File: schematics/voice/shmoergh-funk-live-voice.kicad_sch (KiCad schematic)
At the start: 26 parts, among them Q1 2N3904, U2 TL074, U4 TL074

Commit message: Minor updates
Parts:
- C2: value 270p -> 470p
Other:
- note added: "Discharge RC = 10k * 470pF = 4.7us Could go with 560p too"
- note removed: "Discharge RC = 10k * 270pF = 2.7us"
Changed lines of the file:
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@@
     (effects (font (size 1.27 1.27)) (justify left bottom))
   )
-  (text "Discharge RC = 10k * 270pF = 2.7us" (at 99.06 22.86 0)
+  (text "Discharge RC = 10k * 470pF = 4.7us\nCould go with 560p too"
+    (at 99.06 22.86 0)
     (effects (font (size 1.27 1.27)) (justify left bottom))
   )
@@
       (effects (font (size 1.27 1.27)))
     )
-    (property "Value" "270p" (at 119.38 28.9306 90)
+    (property "Value" "470p" (at 119.38 28.9306 90)
       (effects (font (size 1.27 1.27)))
     )

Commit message: Updated DCO
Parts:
- C2: value 470p -> 560
- R15: value 5.6k -> 20k
- R16: value 20k -> 10k
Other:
- note added: "Integrator's RC constant for max frequency of 5kHz RC = 1 / 5kHz = 0.2ms If any of these components are changed then the code should also be updated (the PWM's output is calculated with a max frequency that's set by these components)."
- note added: "Integrator's discharge constant RCdis = 2.2k * 1nF = 2.2us"
- note added: "Output = 6Vpp"
- note added: "Output aplification A = 1+1 = 2 to have 6.6Vpp"
- note removed: "Integrator's RC constant for max frequency of 5kHz RC = 1 / 5kHz = 0.2ms Integrator's discharge constant RCdis = 2.2k * 1nF = 2.2us"
- note removed: "Output aplification A = 10/3.3 = 3.03 to have 10Vpp"
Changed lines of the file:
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@@
   (junction (at 158.75 77.47) (diameter 0) (color 0 0 0 0)
   )
+  (junction (at 190.5 91.44) (diameter 0) (color 0 0 0 0)
+  )
+  (junction (at 35.56 176.53) (diameter 0) (color 0 0 0 0)
+  )
+  (junction (at 128.27 33.02) (diameter 0) (color 0 0 0 0)
+  )
+  (junction (at 149.86 135.89) (diameter 0) (color 0 0 0 0)
+  )
   (junction (at 158.75 88.9) (diameter 0) (color 0 0 0 0)
-  )
-  (junction (at 190.5 91.44) (diameter 0) (color 0 0 0 0)
-  )
-  (junction (at 35.56 176.53) (diameter 0) (color 0 0 0 0)
-  )
-  (junction (at 128.27 33.02) (diameter 0) (color 0 0 0 0)
-  )
-  (junction (at 149.86 135.89) (diameter 0) (color 0 0 0 0)
   )
   (junction (at 196.85 133.35) (diameter 0) (color 0 0 0 0)
@@
     (stroke (width 0) (type default))
   )
+  (polyline (pts (xy 149.86 66.04) (xy 149.86 67.31))
+    (stroke (width 0) (type dash))
+  )
   (wire (pts (xy 127 124.46) (xy 133.35 124.46))
     (stroke (width 0) (type default))
@@
     (stroke (width 0) (type default))
   )
+  (wire (pts (xy 158.75 88.9) (xy 175.26 88.9))
+    (stroke (width 0) (type default))
+  )
   (wire (pts (xy 224.79 29.21) (xy 251.46 29.21))
     (stroke (width 0) (type default))
@@
     (stroke (width 0) (type default))
   )
+  (polyline (pts (xy 130.81 77.47) (xy 130.81 99.06))
+    (stroke (width 0) (type dash))
+  )
   (wire (pts (xy 175.26 100.33) (xy 175.26 104.14))
     (stroke (width 0) (type default))
@@
     (stroke (width 0) (type default))
   )
+  (wire (pts (xy 128.27 43.18) (xy 128.27 45.72))
+    (stroke (width 0) (type default))
+  )
+  (wire (pts (xy 246.38 41.91) (xy 251.46 41.91))
+    (stroke (width 0) (type default))
+  )
+  (wire (pts (xy 158.75 130.81) (xy 158.75 105.41))
+    (stroke (width 0) (type default))
+  )
+  (wire (pts (xy 158.75 77.47) (xy 158.75 62.23))
+    (stroke (width 0) (type default))
+  )
+  (wire (pts (xy 86.36 83.82) (xy 86.36 86.36))
+    (stroke (width 0) (type default))
+  )
+  (wire (pts (xy 229.87 33.02) (xy 229.87 31.75))
+    (stroke (width 0) (type default))
+  )
+  (wire (pts (xy 194.31 133.35) (xy 196.85 133.35))
+    (stroke (width 0) (type default))
+  )
+  (wire (pts (xy 107.95 33.02) (xy 115.57 33.02))
+    (stroke (width 0) (type default))
+  )
+  (wire (pts (xy 224.79 33.02) (xy 224.79 29.21))
+    (stroke (width 0) (type default))
+  )
+  (wire (pts (xy 144.78 44.45) (xy 140.97 44.45))
+    (stroke (width 0) (type default))
+  )
+  (wire (pts (xy 110.49 66.04) (xy 106.68 66.04))
+    (stroke (width 0) (type default))
+  )
+  (wire (pts (xy 154.94 44.45) (xy 158.75 44.45))
+    (stroke (width 0) (type default))
+  )
+  (wire (pts (xy 106.68 66.04) (xy 106.68 72.39))
+    (stroke (width 0) (type default))
+  )
+  (polyline (pts (xy 124.46 67.31) (xy 149.86 67.31))
+    (stroke (width 0) (type dash))
+  )
+  (wire (pts (xy 134.62 74.93) (xy 140.97 74.93))
+    (stroke (width 0) (type default))
+  )
+  (wire (pts (xy 97.79 72.39) (xy 106.68 72.39))
+    (stroke (width 0) (type default))
+  )
+  (wire (pts (xy 196.85 133.35) (xy 196.85 135.89))
+    (stroke (width 0) (type default))
+  )
+  (wire (pts (xy 246.38 49.53) (xy 251.46 49.53))
+    (stroke (width 0) (type default))
+  )
+  (wire (pts (xy 196.85 133.35) (xy 207.01 133.35))
+    (stroke (width 0) (type default))
+  )
+  (wire (pts (xy 246.38 44.45) (xy 251.46 44.45))
+    (stroke (width 0) (type default))
+  )
+  (wire (pts (xy 140.97 74.93) (xy 142.24 74.93))
+    (stroke (width 0) (type default))
+  )
+  (wire (pts (xy 140.97 44.45) (xy 140.97 62.23))
+    (stroke (width 0) (type default))
+  )
+  (wire (pts (xy 123.19 33.02) (xy 128.27 33.02))
+    (stroke (width 0) (type default))
+  )
   (wire (pts (xy 158.75 88.9) (xy 158.75 97.79))
     (stroke (width 0) (type default))
   )
-  (wire (pts (xy 128.27 43.18) (xy 128.27 45.72))
-    (stroke (width 0) (type default))
-  )
-  (wire (pts (xy 246.38 41.91) (xy 251.46 41.91))
-    (stroke (width 0) (type default))
-  )
-  (wire (pts (xy 158.75 130.81) (xy 158.75 105.41))
-    (stroke (width 0) (type default))
-  )
-  (wire (pts (xy 158.75 77.47) (xy 158.75 62.23))
-    (stroke (width 0) (type default))
-  )
-  (wire (pts (xy 86.36 83.82) (xy 86.36 86.36))
-    (stroke (width 0) (type default))
-  )
-  (wire (pts (xy 229.87 33.02) (xy 229.87 31.75))
-    (stroke (width 0) (type default))
-  )
-  (wire (pts (xy 158.75 88.9) (xy 175.26 88.9))
-    (stroke (width 0) (type default))
-  )
-  (wire (pts (xy 194.31 133.35) (xy 196.85 133.35))
-    (stroke (width 0) (type default))
-  )
-  (wire (pts (xy 107.95 33.02) (xy 115.57 33.02))
-    (stroke (width 0) (type default))
-  )
-  (wire (pts (xy 224.79 33.02) (xy 224.79 29.21))
-    (stroke (width 0) (type default))
-  )
-  (wire (pts (xy 144.78 44.45) (xy 140.97 44.45))
-    (stroke (width 0) (type default))
-  )
-  (wire (pts (xy 110.49 66.04) (xy 106.68 66.04))
-    (stroke (width 0) (type default))
-  )
-  (wire (pts (xy 154.94 44.45) (xy 158.75 44.45))
-    (stroke (width 0) (type default))
-  )
-  (wire (pts (xy 106.68 66.04) (xy 106.68 72.39))
-    (stroke (width 0) (type default))
-  )
-  (wire (pts (xy 134.62 74.93) (xy 140.97 74.93))
-    (stroke (width 0) (type default))
-  )
-  (wire (pts (xy 97.79 72.39) (xy 106.68 72.39))
-    (stroke (width 0) (type default))
-  )
-  (wire (pts (xy 196.85 133.35) (xy 196.85 135.89))
-    (stroke (width 0) (type default))
-  )
-  (wire (pts (xy 246.38 49.53) (xy 251.46 49.53))
-    (stroke (width 0) (type default))
-  )
-  (wire (pts (xy 196.85 133.35) (xy 207.01 133.35))
-    (stroke (width 0) (type default))
-  )
-  (wire (pts (xy 246.38 44.45) (xy 251.46 44.45))
-    (stroke (width 0) (type default))
-  )
-  (wire (pts (xy 140.97 74.93) (xy 142.24 74.93))
-    (stroke (width 0) (type default))
-  )
-  (wire (pts (xy 140.97 44.45) (xy 140.97 62.23))
-    (stroke (width 0) (type default))
-  )
-  (wire (pts (xy 123.19 33.02) (xy 128.27 33.02))
-    (stroke (width 0) (type default))
-  )
   (wire (pts (xy 128.27 33.02) (xy 133.35 33.02))
     (stroke (width 0) (type default))
@@
   (wire (pts (xy 121.92 74.93) (xy 127 74.93))
     (stroke (width 0) (type default))
+  )
+  (polyline (pts (xy 124.46 99.06) (xy 124.46 67.31))
+    (stroke (width 0) (type dash))
   )
   (wire (pts (xy 118.11 66.04) (xy 121.92 66.04))
@@
     (effects (font (size 1.27 1.27) (thickness 0.254) bold) (justify left bottom))
   )
-  (text "Vmax = 3.3V" (at 160.02 77.47 0)
+  (text "Vmax = 3.3V" (at 154.94 73.66 0)
     (effects (font (size 1.27 1.27)) (justify left bottom))
   )
@@
     (effects (font (size 1.27 1.27) (thickness 0.254) bold) (justify left bottom))
   )
+  (text "Output = 6Vpp" (at 207.01 143.51 0)
+    (effects (font (size 1.27 1.27)) (justify left bottom))
+  )
   (text "0-3.3V" (at 66.04 76.2 0)
     (effects (font (size 1.27 1.27)) (justify left bottom))
@@
     (effects (font (size 1.27 1.27)) (justify left bottom))
   )
-  (text "Output aplification A = 10/3.3 = 3.03\nto have 10Vpp"
-    (at 185.42 109.22 0)
+  (text "Output aplification A = 1+1 = 2\nto have 6.6Vpp" (at 185.42 109.22 0)
     (effects (font (size 1.27 1.27)) (justify left bottom))
   )
-  (text "Integrator's RC constant for  max frequency of 5kHz\nRC = 1 / 5kHz = 0.2ms\n\nIntegrator's discharge constant\nRCdis = 2.2k * 1nF = 2.2us"
+  (text "Integrator's discharge constant\nRCdis = 2.2k * 1nF = 2.2us"
     (at 166.37 53.34 0)
     (effects (font (size 1.27 1.27)) (justify left bottom))
@@
   (text "Discharge RC = 10k * 470pF = 4.7us\nCould go with 560p too"
     (at 99.06 22.86 0)
+    (effects (font (size 1.27 1.27)) (justify left bottom))
+  )
+  (text "Integrator's RC constant for  max frequency of 5kHz\nRC = 1 / 5kHz = 0.2ms\n\nIf any of these components are changed then the \ncode should also be updated (the PWM's output\nis calculated with a max frequency that's set\nby these components)."
+    (at 95.25 114.3 0)
     (effects (font (size 1.27 1.27)) (justify left bottom))
   )
@@
       (effects (font (size 1.27 1.27)))
     )
-    (property "Value" "470p" (at 119.38 28.9306 90)
+    (property "Value" "560" (at 119.38 28.9306 90)
       (effects (font (size 1.27 1.27)))
     )
@@
       (effects (font (size 1.27 1.27)))
     )
-    (property "Value" "20k" (at 182.88 97.79 90)
+    (property "Value" "10k" (at 182.88 97.79 90)
       (effects (font (size 1.27 1.27)))
     )
@@
       (effects (font (size 1.27 1.27)) (justify left))
     )
-    (property "Value" "5.6k" (at 198.628 140.843 0)
+    (property "Value" "20k" (at 198.628 140.843 0)
       (effects (font (size 1.27 1.27)) (justify left))
     )

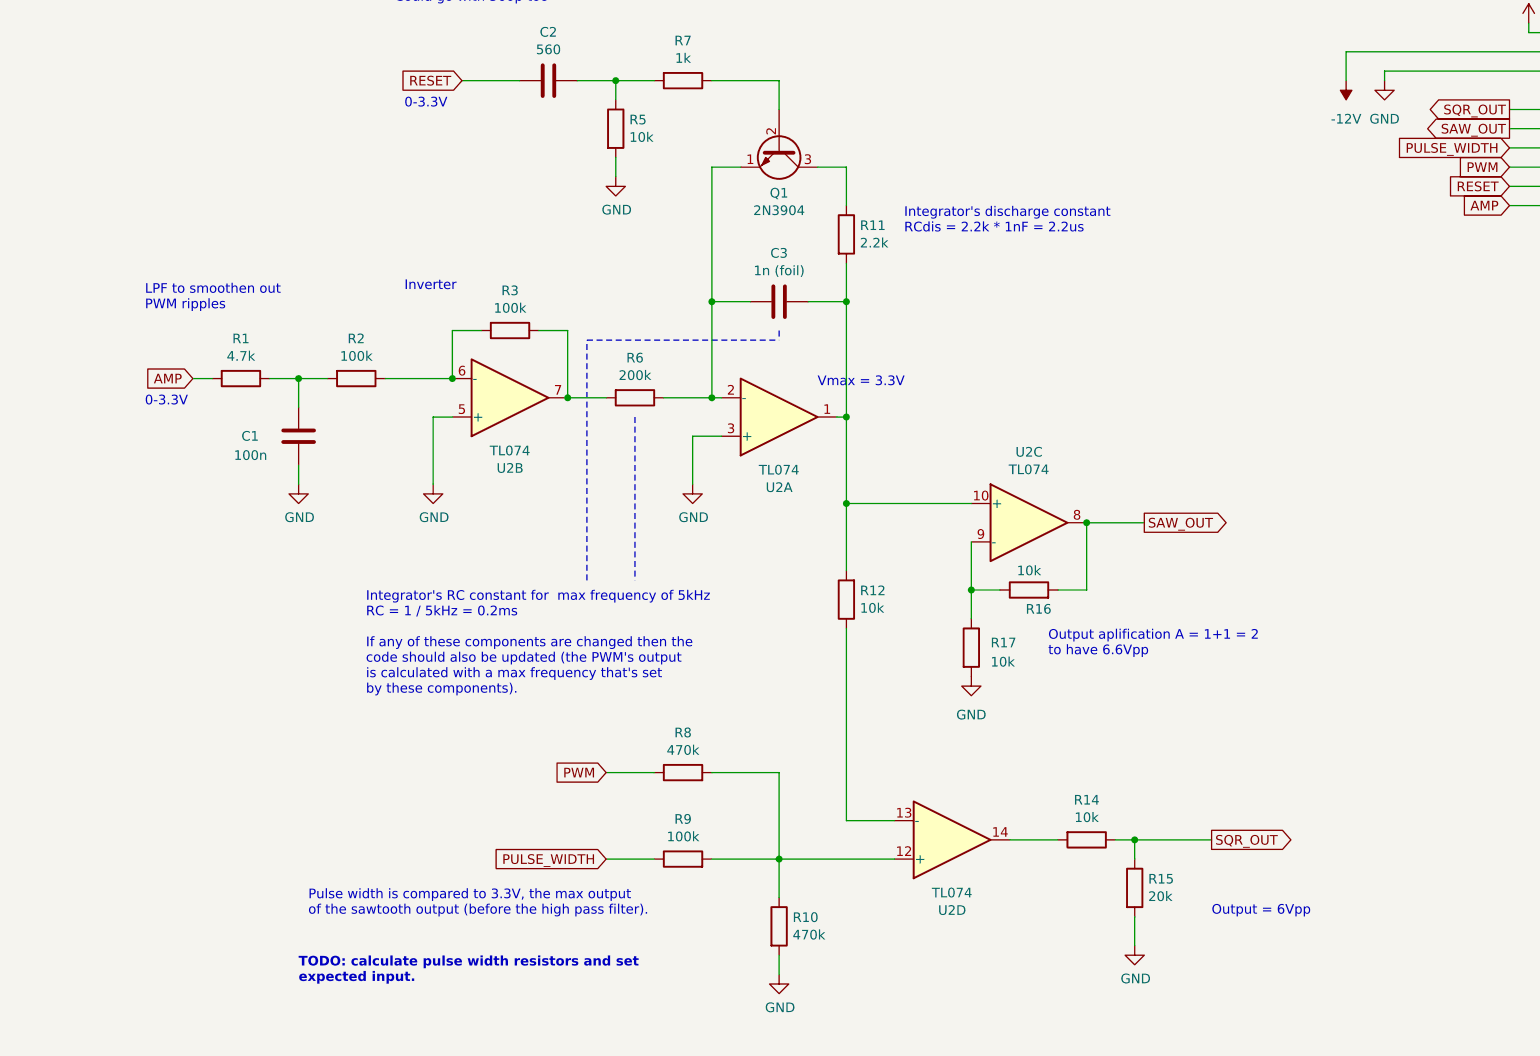
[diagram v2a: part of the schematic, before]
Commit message: DCO schematic update
Changed the DCO design from using a PNP transistor for the switch,
positive charge and an inverting amp with bias for the saw output. This
allows to bias the sawtooth output to oscillate around 0V which makes
possible to set precise pulse width values for all voices regardless of
potential component differences. Also, this eventually needs less
component altogether.
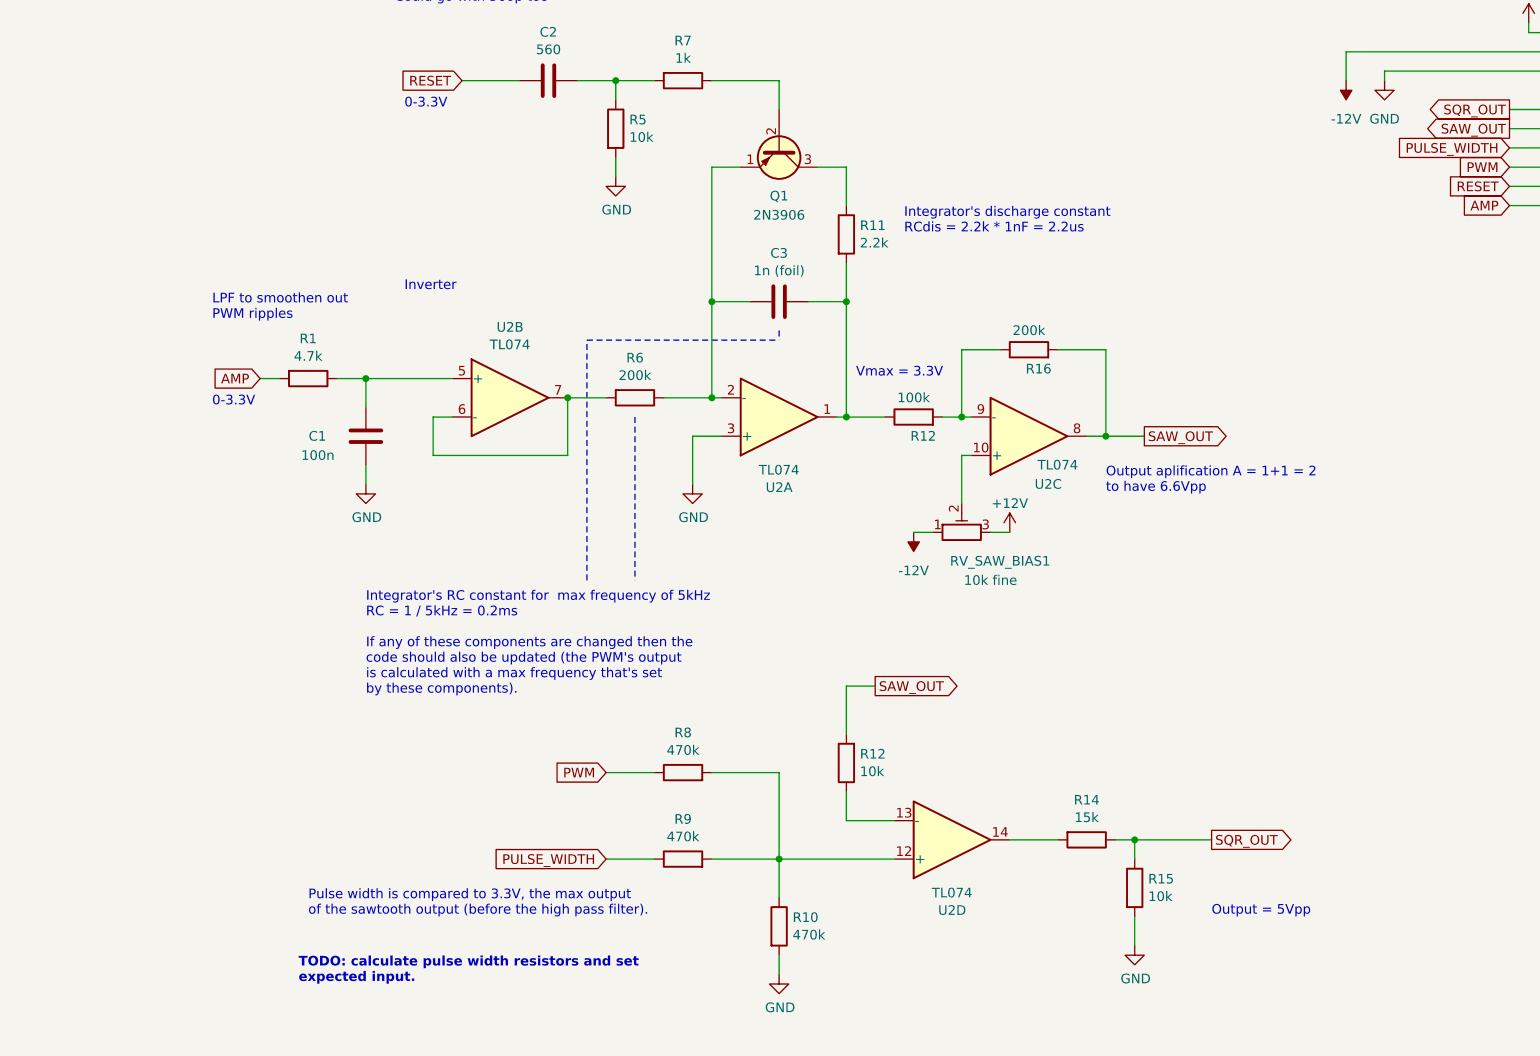
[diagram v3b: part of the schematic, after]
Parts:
- removed Q1: 2N3904, Package_TO_SOT_THT:TO-92_Wide, symbol Transistor_BJT:2N3904
- removed R17: 10k, Shmoergh_Custom_Footprints:R_Axial_DIN0207_L6.3mm_D2.5mm_P7.62mm_Horizontal, symbol Device:R
- removed R2, R3: 100k, Shmoergh_Custom_Footprints:R_Axial_DIN0207_L6.3mm_D2.5mm_P7.62mm_Horizontal, symbol Device:R
- added Q1: 2N3906, Package_TO_SOT_THT_AKL:TO-92_Inline_Wide_EBC, symbol PCM_Transistor_BJT_AKL:2N3906
- added R12: 100k, Shmoergh_Custom_Footprints:R_Axial_DIN0207_L6.3mm_D2.5mm_P7.62mm_Horizontal, symbol Device:R
- added RV_SAW_BIAS1: 10k fine, symbol Device:R_Potentiometer_Trim
- R14: value 10k -> 15k
- R15: value 20k -> 10k
- R16: value 10k -> 200k
- R9: value 100k -> 470k
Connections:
- net +12V: now also RV_SAW_BIAS1.3
- net -12V: now also RV_SAW_BIAS1.1
- net GND: no longer U2.5 (+)
- net SAW_OUT: now also R12.2
- net at R16.1, U2.9 (-): now also R12.2
- net at R6.2, U2.7: now also U2.6 (-)
- net at C3.1, R11.2, U2.1: now also R12.1; no longer R12.2, U2.10 (+)
- net at C3.2, R6.1, U2.2 (-): now also Q1.1 (E)
- net at R7.1: now also Q1.2 (B)
- net at R11.1: now also Q1.3 (C)
- net at C1.1, R1.1: now also U2.5 (+)
- new net: RV_SAW_BIAS1.2, U2.10 (+)
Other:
- note added: "Output = 5Vpp"
- note removed: "Output = 6Vpp"
- moved on the sheet: C1, R1, R12, R16, U2C
